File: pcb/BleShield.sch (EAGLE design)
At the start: 28 parts, among them SW1 SPST_TACT-EVQQ2, SW2 SPST_TACT-EVQQ2, U1 ARDUINO_SHIELDNOHOLES, Y1 32.768KHz, 10 PPM

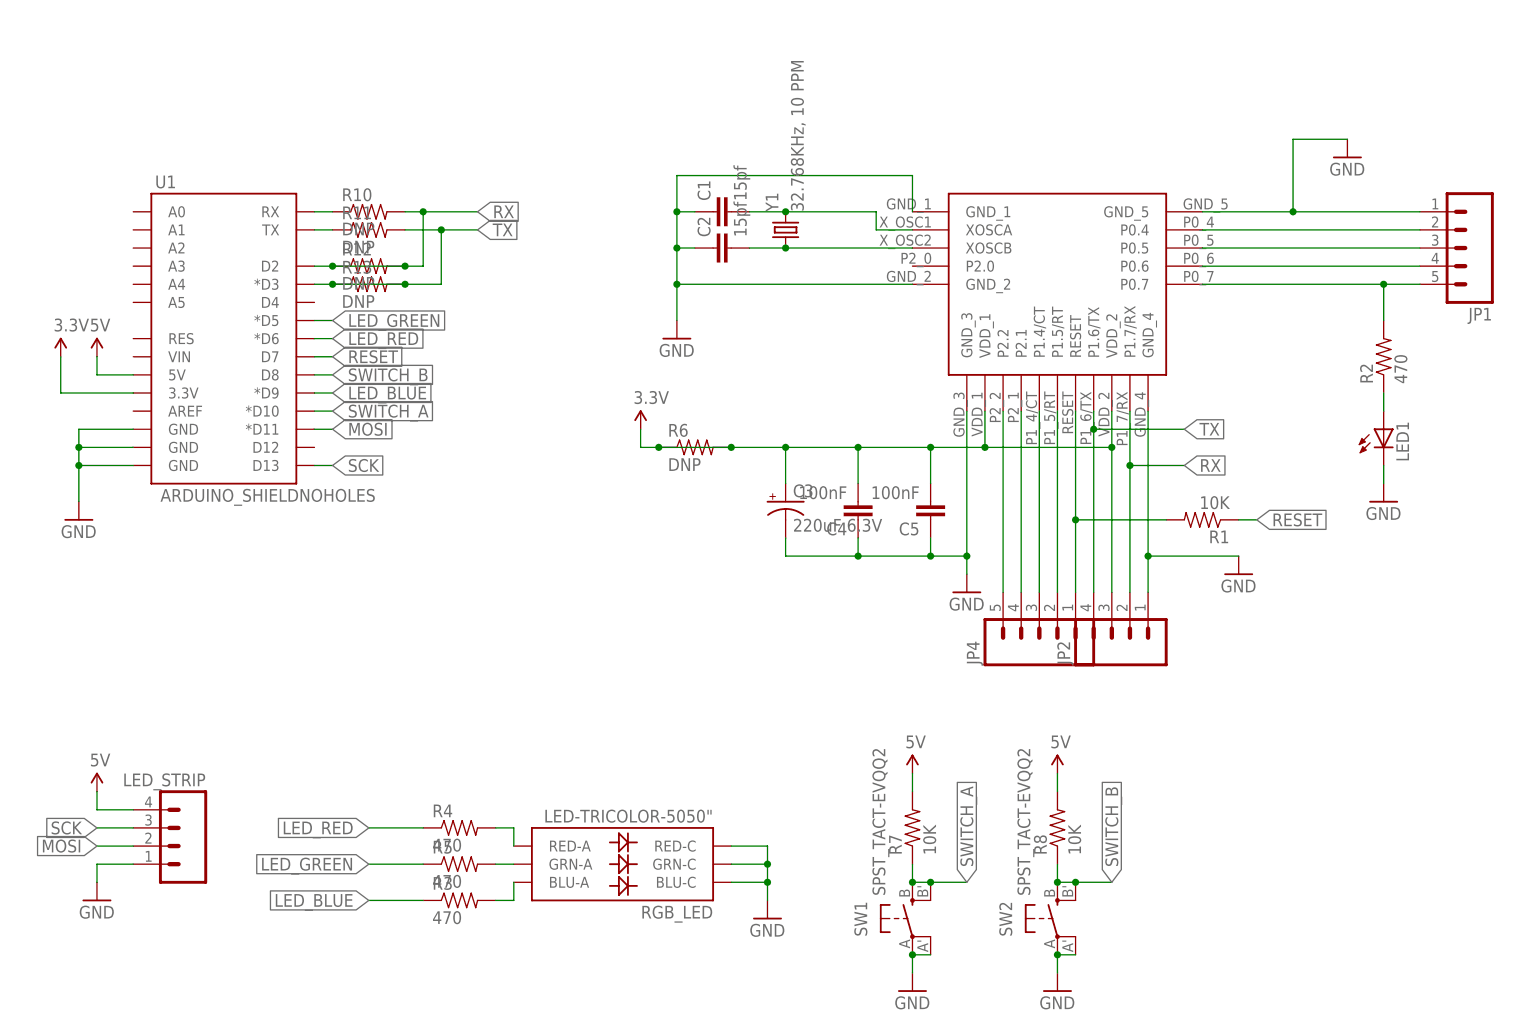
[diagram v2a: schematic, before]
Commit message: Fix RX/TX line assignment
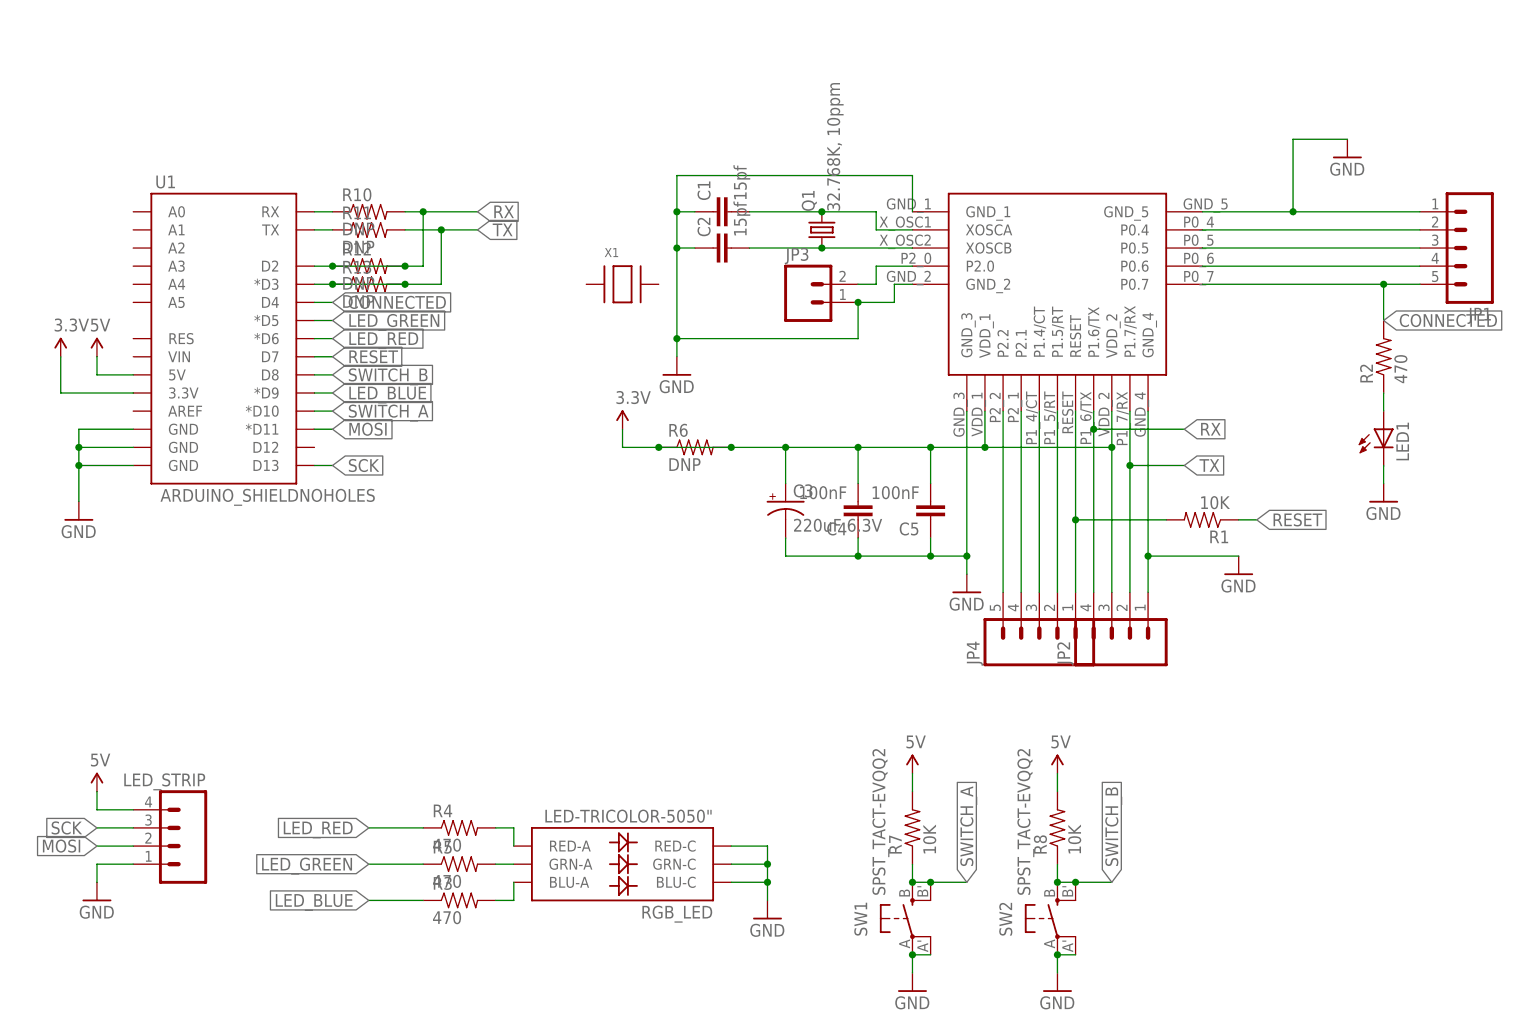
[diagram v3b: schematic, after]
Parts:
- removed Y1: 32.768KHz, 10 PPM, blinkiverse:CRYSTAL
- added JP3: (no value), BLE:M02
- added Q1: 32.768K, 10ppm, blinkiverse:CRYSTAL3215
- added X1: (no value), adafruit:XTAL-3.2X1.5
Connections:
- removed net N$9: JP1.5, R2.2, U$1.P0.7
- new net CONNECTED: JP1.5, R2.2, U$1.P0.7, U1.D4
- new net N$19: JP3.2, U$1.P2.0
- net GND: now also JP3.1
- net N$3: now also Q1.2; no longer Y1.2
- net N$4: now also Q1.1; no longer Y1.1
- net RX: now also JP2.4, U$1.P1.6/TX; no longer JP2.2, U$1.P1.7/RX
- net TX: now also JP2.2, U$1.P1.7/RX; no longer JP2.4, U$1.P1.6/TX

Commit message: RevC release candidate
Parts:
- removed X1: (no value), adafruit:XTAL-3.2X1.5
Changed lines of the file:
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@@
 <part name="JP3" library="BLE" deviceset="M02" device=""/>
 <part name="Q1" library="blinkiverse" deviceset="CRYSTAL" device="3215" value="32.768K, 10ppm"/>
-<part name="X1" library="adafruit" deviceset="XTAL" device="-3.2X1.5"/>
 </parts>
 <sheets>
@@
 <instance part="JP3" gate="G$1" x="119.38" y="104.14"/>
 <instance part="Q1" gate="G$1" x="121.92" y="114.3" rot="R90"/>
-<instance part="X1" gate="G$1" x="93.98" y="106.68"/>
 </instances>
 <busses>

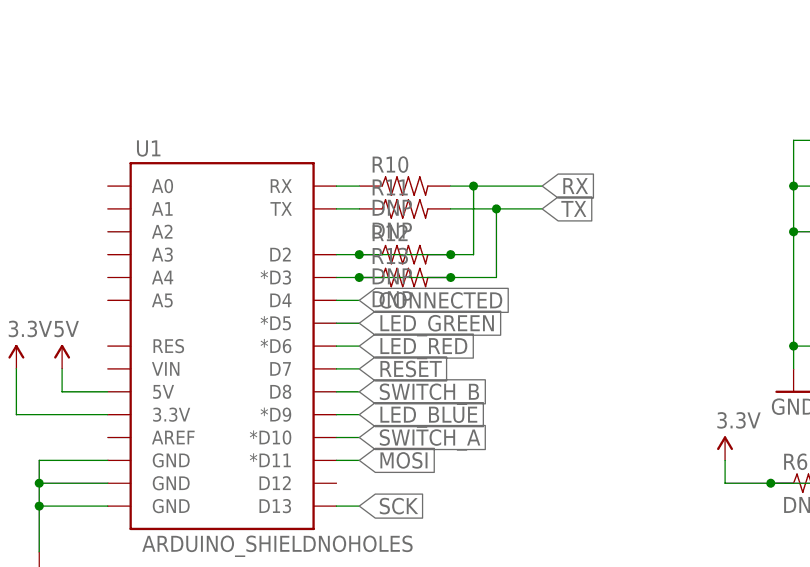
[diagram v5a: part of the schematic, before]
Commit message: Add 47K resistor to work around the voltage difference problem
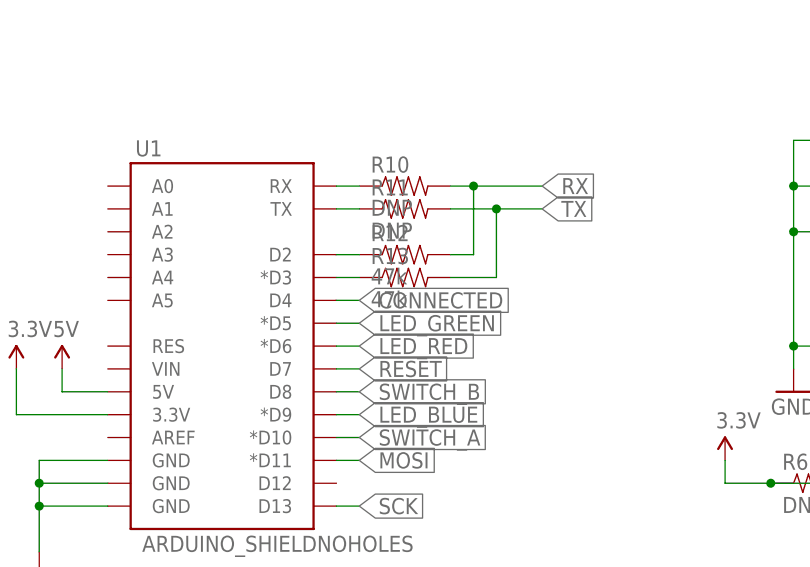
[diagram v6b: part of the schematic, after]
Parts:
- R12, R13: value DNP -> 47k
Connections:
- new net N$20: R13.1, U1.*D3
- new net N$9: R12.1, U1.D2
- net RX: no longer R12.1, U1.D2
- net TX: no longer R13.1, U1.*D3
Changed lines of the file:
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@@
 <part name="R10" library="SparkFun" deviceset="RESISTOR" device="0805-RES" value="DNP"/>
 <part name="R11" library="SparkFun" deviceset="RESISTOR" device="0805-RES" value="DNP"/>
-<part name="R12" library="SparkFun" deviceset="RESISTOR" device="0805-RES" value="DNP"/>
-<part name="R13" library="SparkFun" deviceset="RESISTOR" device="0805-RES" value="DNP"/>
+<part name="R12" library="SparkFun" deviceset="RESISTOR" device="0805-RES" value="47k"/>
+<part name="R13" library="SparkFun" deviceset="RESISTOR" device="0805-RES" value="47k"/>
 <part name="JP1" library="SparkFun" deviceset="M05" device="1.27MM"/>
 <part name="JP2" library="SparkFun" deviceset="M04" device="1.27MM"/>
@@
 <wire x1="66.04" y1="109.22" x2="66.04" y2="116.84" width="0.1524" layer="91"/>
 <junction x="66.04" y="116.84"/>
-<pinref part="U1" gate="G$1" pin="D2"/>
-<pinref part="R12" gate="G$1" pin="1"/>
-<wire x1="50.8" y1="109.22" x2="53.34" y2="109.22" width="0.1524" layer="91"/>
-<wire x1="53.34" y1="109.22" x2="63.5" y2="109.22" width="0.1524" layer="91"/>
-<junction x="53.34" y="109.22"/>
-<junction x="63.5" y="109.22"/>
 </segment>
 <segment>
@@
 <wire x1="68.58" y1="106.68" x2="68.58" y2="114.3" width="0.1524" layer="91"/>
 <junction x="68.58" y="114.3"/>
-<pinref part="U1" gate="G$1" pin="*D3"/>
-<pinref part="R13" gate="G$1" pin="1"/>
-<wire x1="50.8" y1="106.68" x2="53.34" y2="106.68" width="0.1524" layer="91"/>
-<wire x1="63.5" y1="106.68" x2="53.34" y2="106.68" width="0.1524" layer="91"/>
-<junction x="53.34" y="106.68"/>
-<junction x="63.5" y="106.68"/>
 </segment>
 <segment>
@@
 </segment>
 </net>
+<net name="N$9" class="0">
+<segment>
+<pinref part="R12" gate="G$1" pin="1"/>
+<pinref part="U1" gate="G$1" pin="D2"/>
+<wire x1="50.8" y1="109.22" x2="53.34" y2="109.22" width="0.1524" layer="91"/>
+</segment>
+</net>
+<net name="N$20" class="0">
+<segment>
+<pinref part="R13" gate="G$1" pin="1"/>
+<pinref part="U1" gate="G$1" pin="*D3"/>
+<wire x1="50.8" y1="106.68" x2="53.34" y2="106.68" width="0.1524" layer="91"/>
+</segment>
+</net>

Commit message: Update library name
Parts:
- Q1: device blinkiverse:CRYSTAL3215 -> blinkinlabs:CRYSTAL3215
- RGB_LED: device blinkiverse:LED-TRICOLOR-5050" -> blinkinlabs:LED-TRICOLOR-5050"
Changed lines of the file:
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@@
 <part name="R8" library="SparkFun" deviceset="RESISTOR" device="0805-RES" value="10K"/>
 <part name="GND9" library="SparkFun" deviceset="GND" device=""/>
-<part name="RGB_LED" library="blinkiverse" deviceset="LED-TRICOLOR-5050" device="&quot;"/>
+<part name="RGB_LED" library="blinkinlabs" deviceset="LED-TRICOLOR-5050" device="&quot;"/>
 <part name="LED1" library="adafruit" deviceset="LED" device="CHIPLED_0805"/>
 <part name="R2" library="SparkFun" deviceset="RESISTOR" device="0805-RES" value="470"/>
@@
 <part name="SW2" library="adafruit" deviceset="SPST_TACT" device="-EVQQ2"/>
 <part name="JP3" library="BLE" deviceset="M02" device=""/>
-<part name="Q1" library="blinkiverse" deviceset="CRYSTAL" device="3215" value="32.768K, 10ppm"/>
+<part name="Q1" library="blinkinlabs" deviceset="CRYSTAL" device="3215" value="32.768K, 10ppm"/>
 </parts>
 <sheets>
